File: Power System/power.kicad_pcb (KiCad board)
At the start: 2 copper layers, 139.7 x 100.3 mm, 35 parts, among them J1 PC104_40Pin_2.54mm, J2 Charge Cable, J3 Battery Pack, J4 IDC Header, U1 ds2781e+

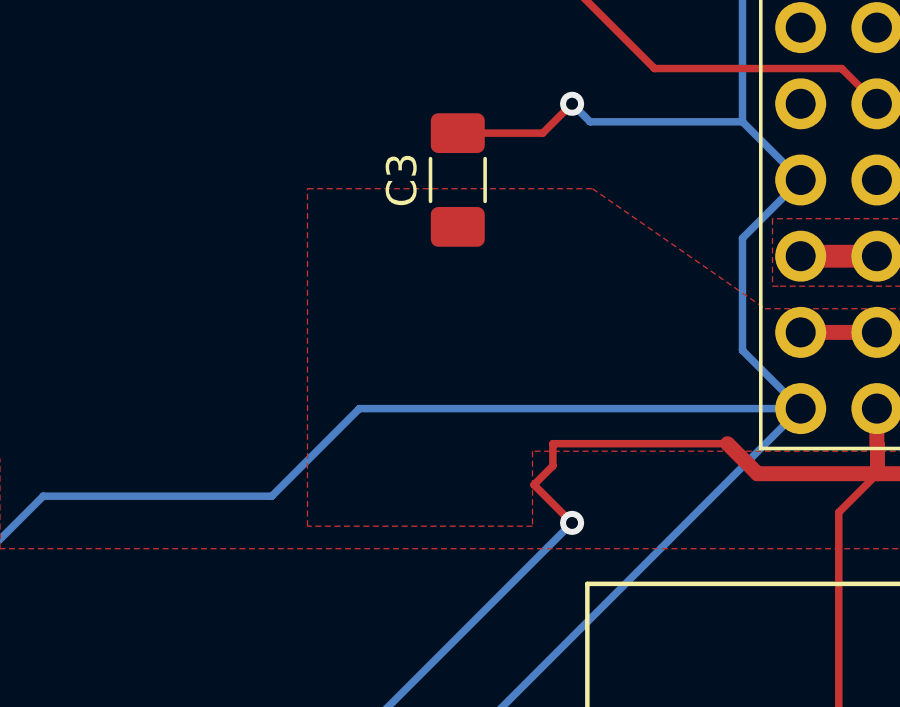
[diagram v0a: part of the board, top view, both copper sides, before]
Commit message: Further resized fill zones...
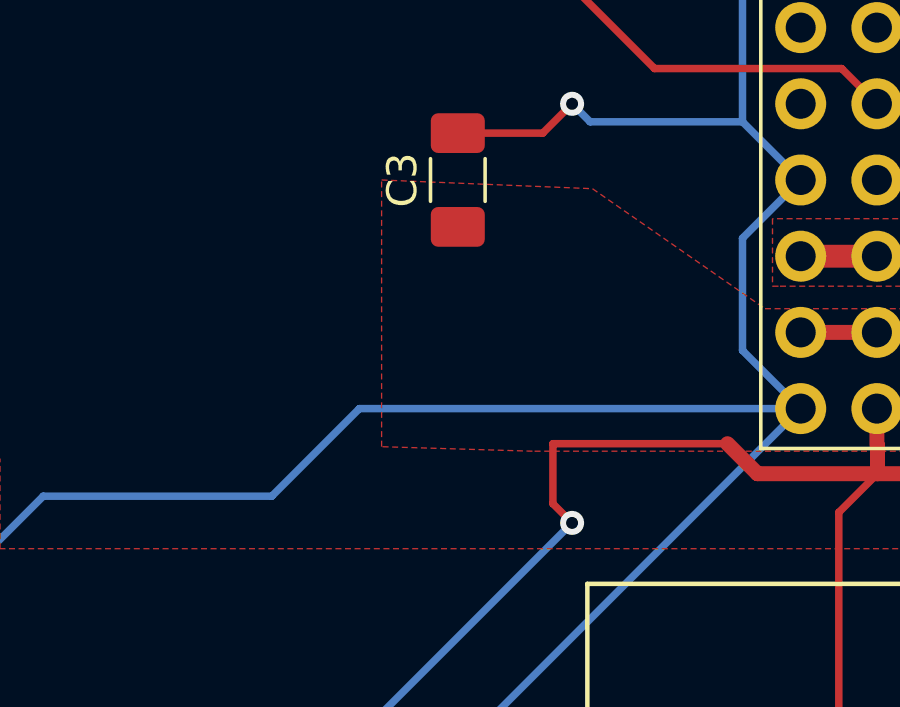
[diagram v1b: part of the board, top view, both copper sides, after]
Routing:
- net +3V3: track 156.1 -> 155.5 mm
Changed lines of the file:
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@@
     (thickness 1.6)
     (drawings 14)
-    (tracks 248)
+    (tracks 247)
     (zones 0)
     (modules 35)
@@
   (segment (start 159.5 101.75) (end 158.75 102.5) (width 0.5) (layer F.Cu) (net 23))
   (segment (start 153.5 102.5) (end 152.5 101.5) (width 0.5) (layer F.Cu) (net 23))
-  (segment (start 152.5 101.5) (end 146.68 101.5) (width 0.25) (layer F.Cu) (net 23))
   (segment (start 157.5 101.552081) (end 157.5 102.5) (width 0.5) (layer F.Cu) (net 23))
   (segment (start 157.48 101.532081) (end 157.5 101.552081) (width 0.25) (layer F.Cu) (net 23))
@@
   (via (at 147.32 104.14) (size 0.8) (drill 0.4) (layers F.Cu B.Cu) (net 23))
   (segment (start 138.5 112.96) (end 147.32 104.14) (width 0.25) (layer B.Cu) (net 23))
-  (segment (start 147.32 104.14) (end 146.05 102.87) (width 0.25) (layer F.Cu) (net 23))
-  (segment (start 146.68 101.5) (end 146.68 102.24) (width 0.25) (layer F.Cu) (net 23))
-  (segment (start 146.68 102.24) (end 146.05 102.87) (width 0.25) (layer F.Cu) (net 23))
+  (segment (start 146.68 103.5) (end 147.32 104.14) (width 0.25) (layer F.Cu) (net 23))
+  (segment (start 146.68 101.5) (end 146.68 103.5) (width 0.25) (layer F.Cu) (net 23))
+  (segment (start 152.5 101.5) (end 146.68 101.5) (width 0.25) (layer F.Cu) (net 23))
   (segment (start 42 67.5) (end 37.75 63.25) (width 0.25) (layer F.Cu) (net 24) (status 20))
   (segment (start 42 73.25) (end 42 67.5) (width 0.25) (layer F.Cu) (net 24))
@@
     (polygon
       (pts
-        (xy 138.5 104.25) (xy 138.5 93) (xy 148 93) (xy 153.75 97) (xy 158.75 97)
-        (xy 158.75 101.75) (xy 146 101.75) (xy 146 104.25)
+        (xy 140.97 101.6) (xy 140.97 92.71) (xy 148 93) (xy 153.75 97) (xy 158.75 97)
+        (xy 158.75 101.75) (xy 146 101.75)
       )
     )

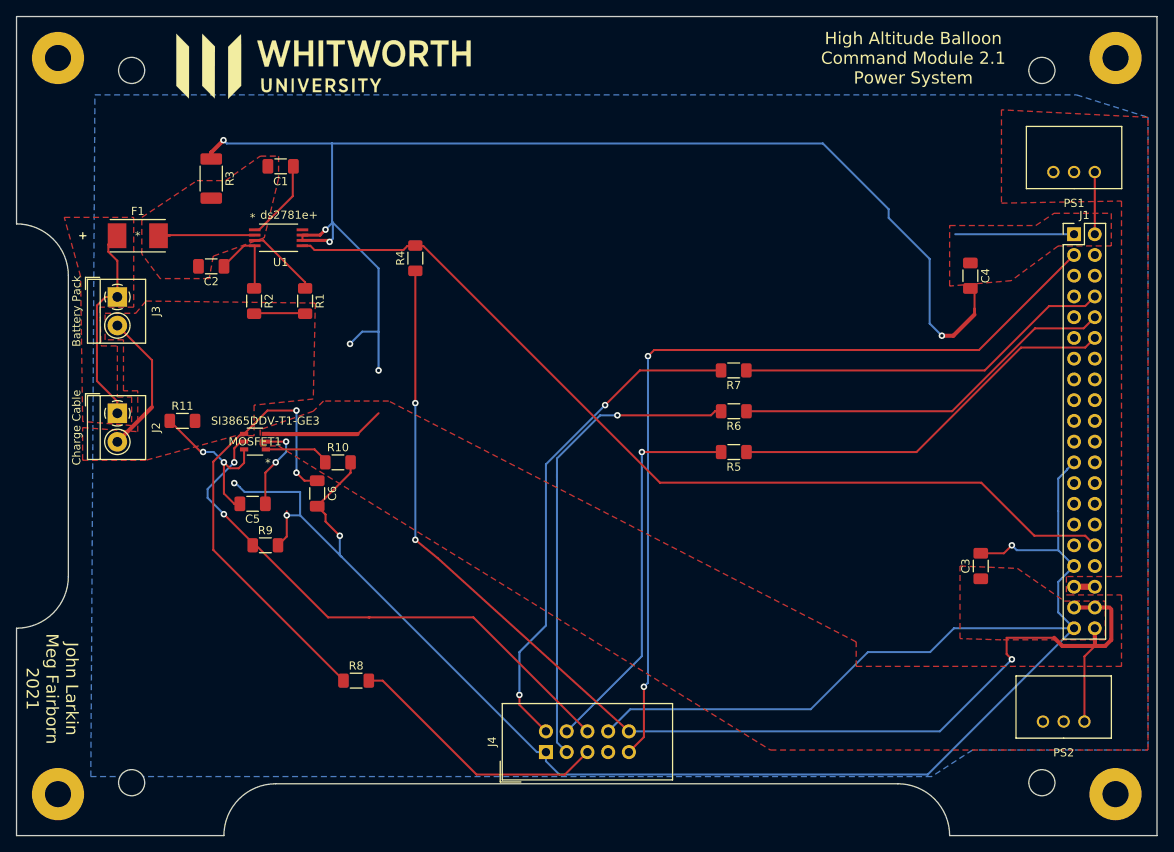
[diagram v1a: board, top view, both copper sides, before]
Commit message: Pretty sure power system fill zones are done
I don't know why it wants to commit changes to the schematic?
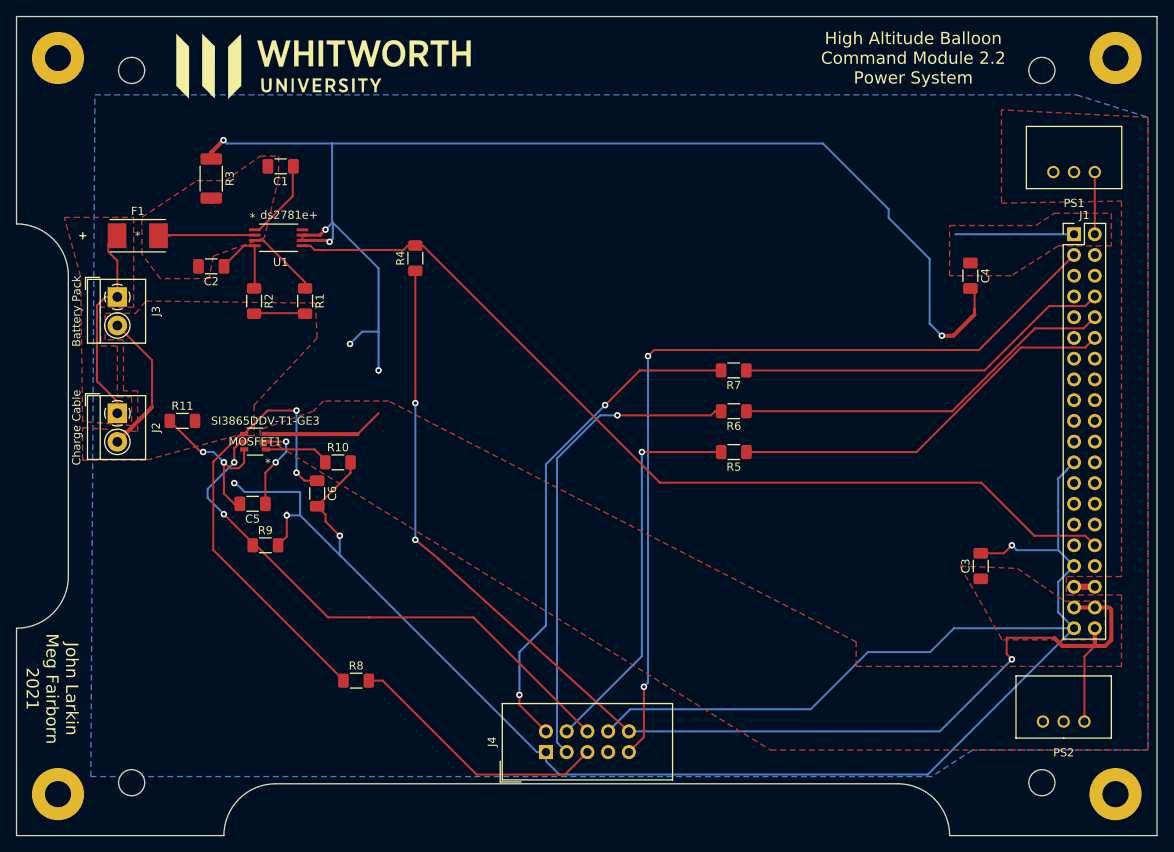
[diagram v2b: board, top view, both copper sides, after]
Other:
- board text added: "High Altitude Balloon Command Module 2.2 Power System"
- board text removed: "High Altitude Balloon Command Module 2.1 Power System"

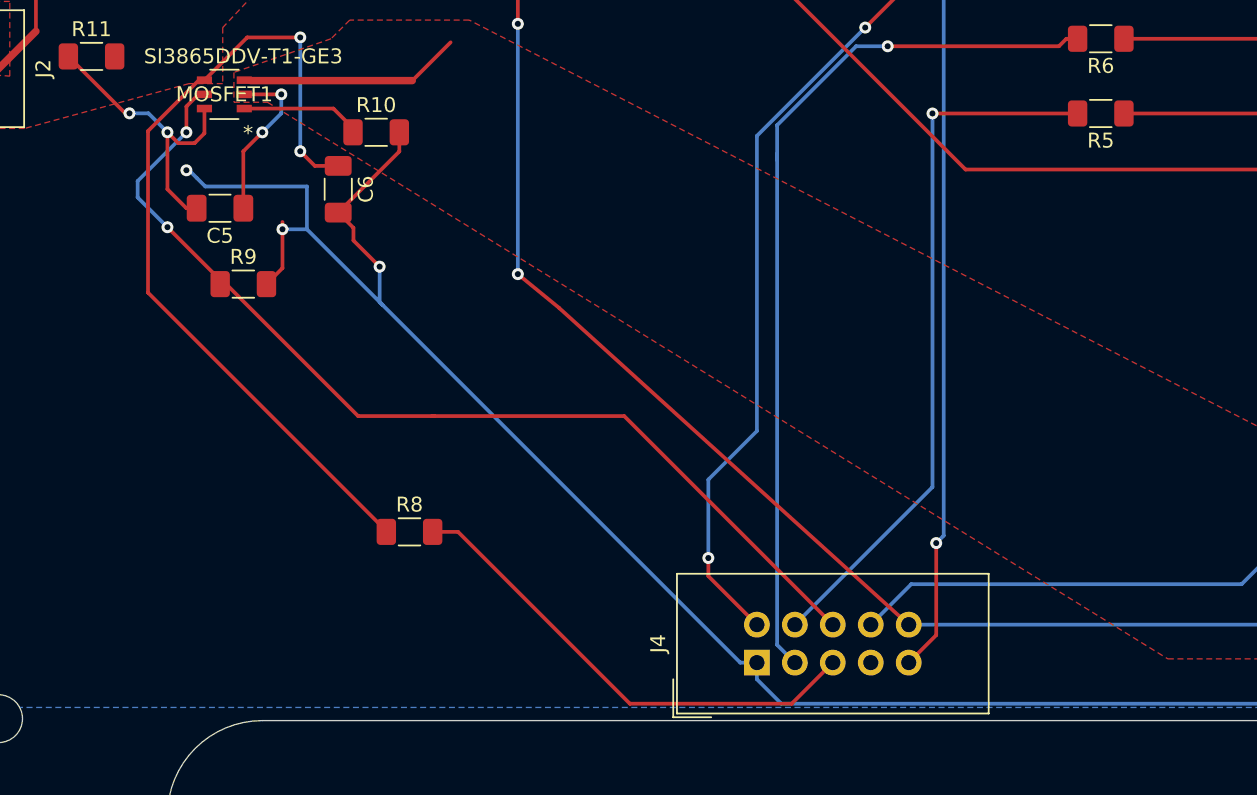
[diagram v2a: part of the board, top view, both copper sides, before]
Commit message: moved components away from each other
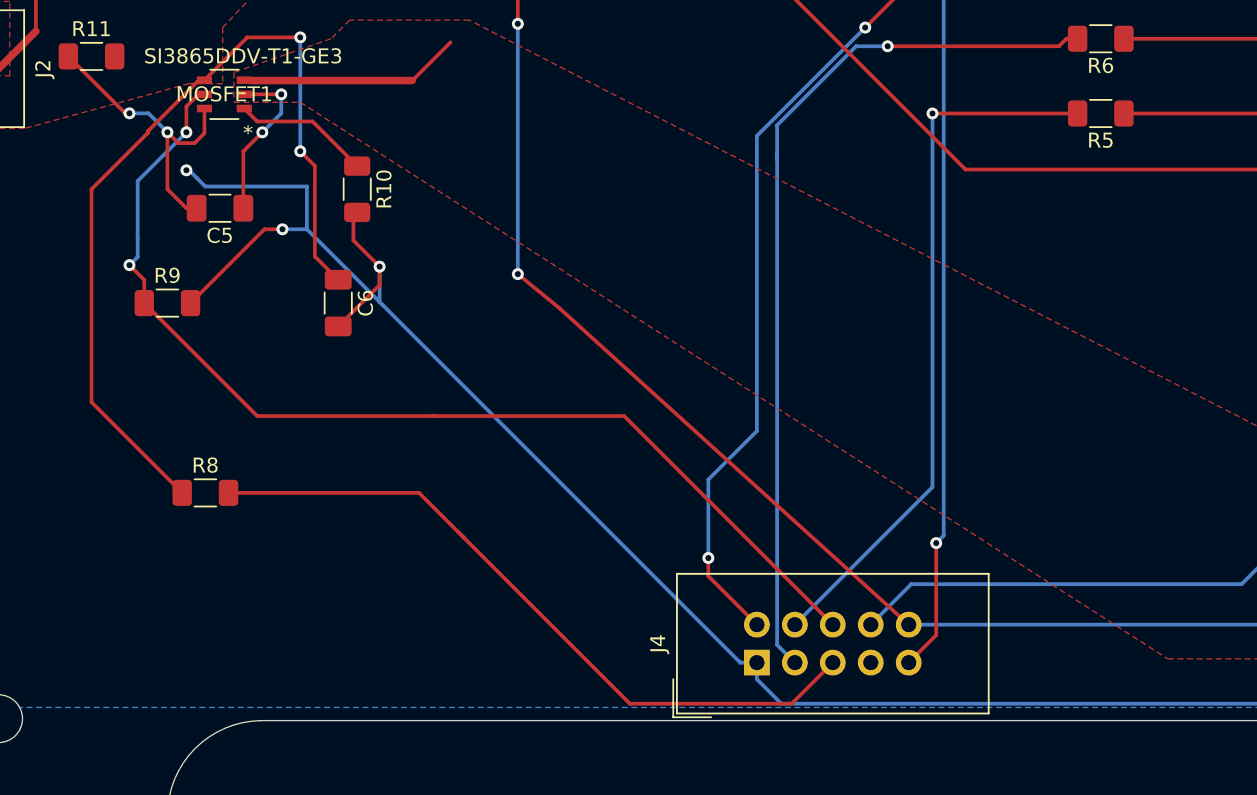
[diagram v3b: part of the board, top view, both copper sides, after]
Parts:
- moved R8 13.9 mm to (53.3, 104.1)
- moved C6 7.62 mm to (62.2, 91.4)
- moved R9 5.24 mm to (50.8, 91.4)
- moved R10 4.02 mm to (63.5, 83.8), turned to 270 degrees
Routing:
- net Net-(J4-Pad5): track 32.7 -> 48.0 mm
- net /PWR_ENABLE: track 67.7 -> 71.9 mm
- net +BATT: track 80.4 -> 82.0 mm
- net GND: track 419.2 -> 420.3 mm
- net Net-(MOSFET1-Pad1): track 8.10 -> 9.15 mm

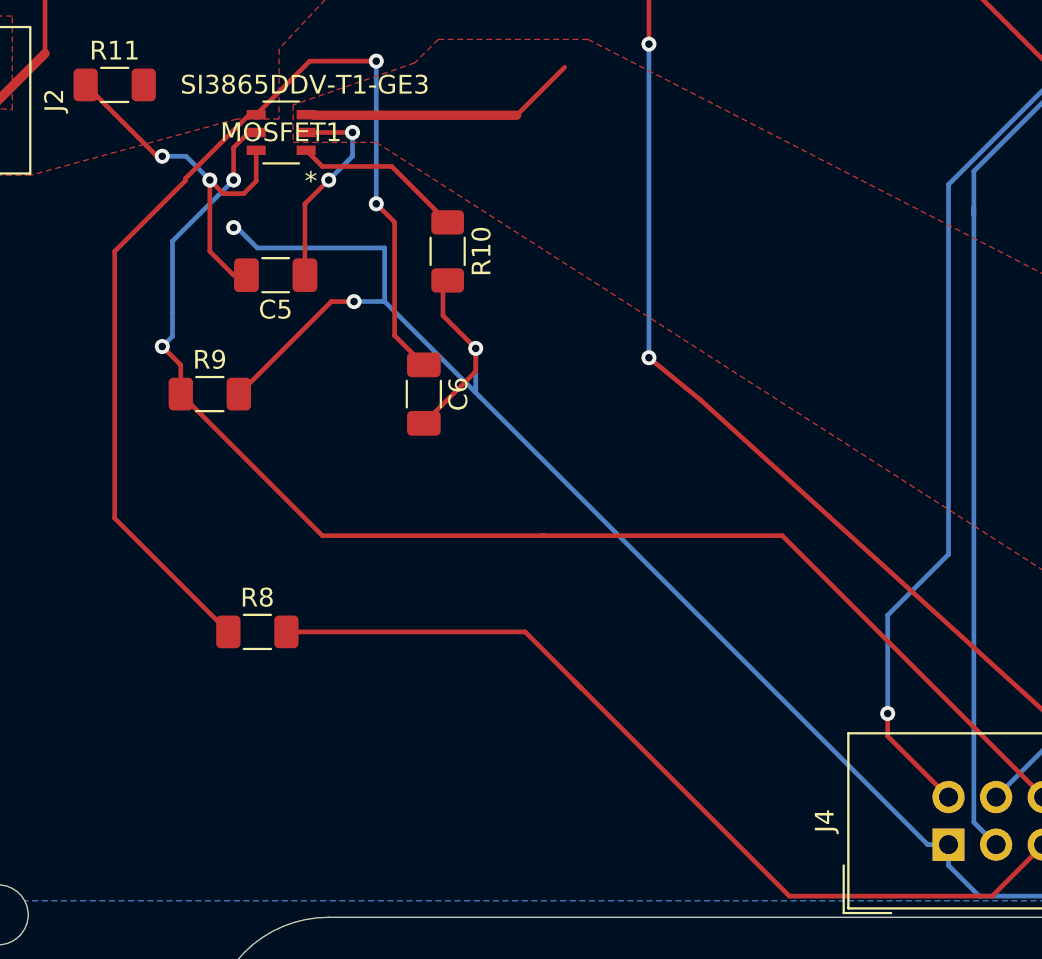
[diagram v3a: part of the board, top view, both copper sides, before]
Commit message: moved C6 a little more and changed track layout a little
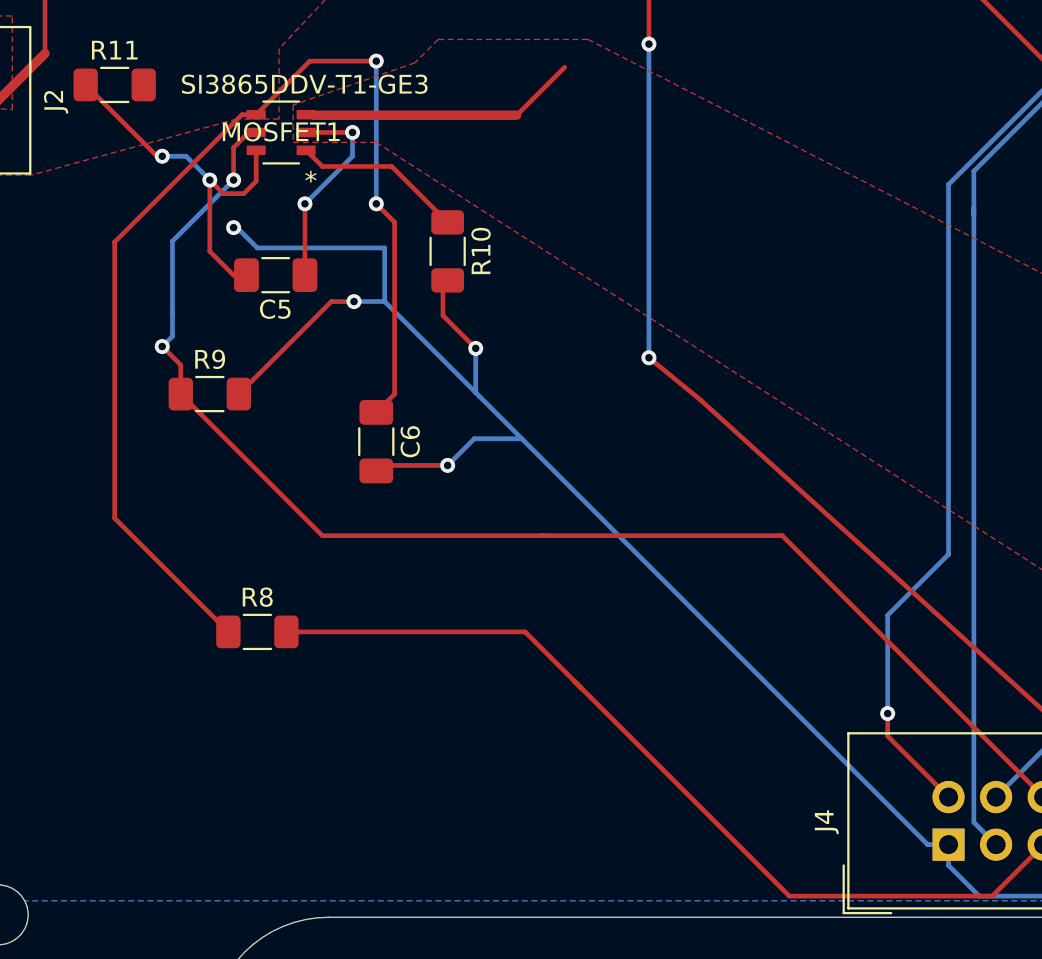
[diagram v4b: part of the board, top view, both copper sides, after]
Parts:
- moved C6 3.59 mm to (59.7, 94.0)
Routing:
- net GND: track 420.3 -> 423.7 mm, vias 10 -> 11
- net +BATT: track 82.0 -> 84.9 mm

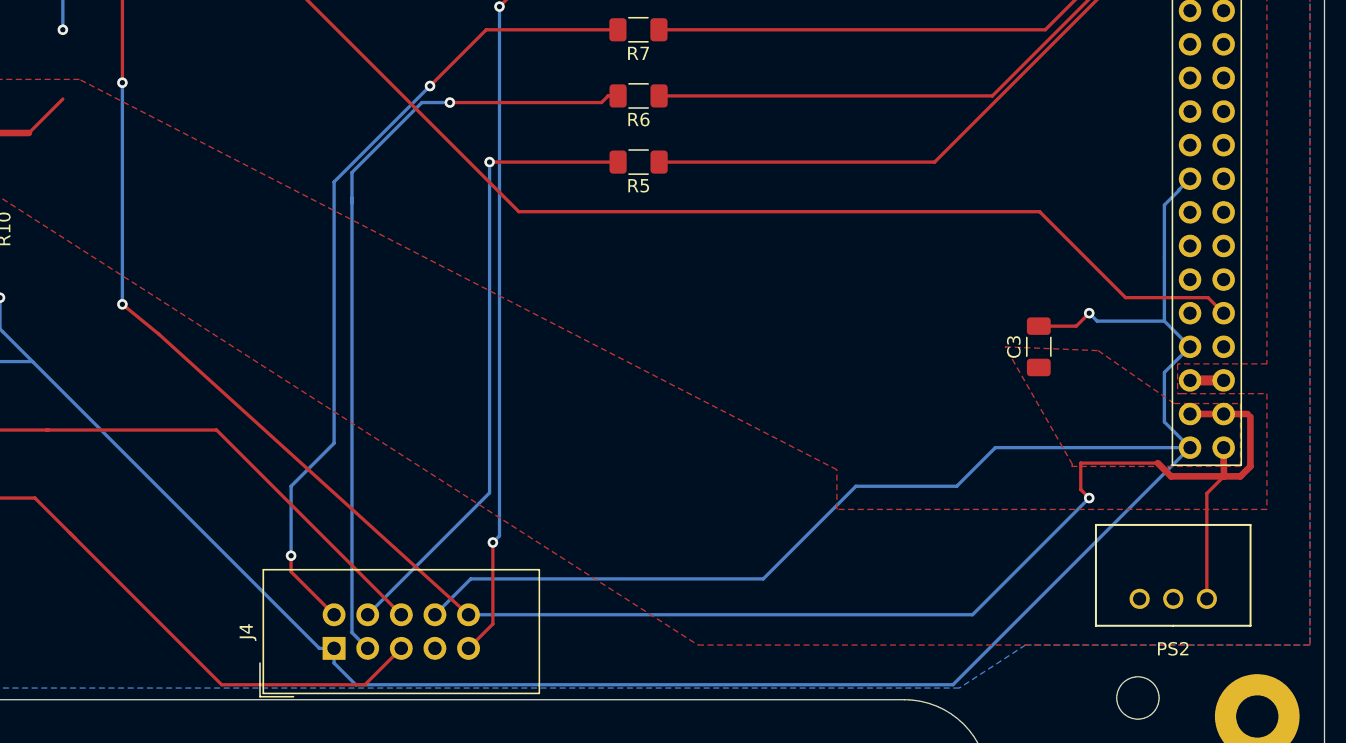
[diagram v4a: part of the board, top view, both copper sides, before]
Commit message: Improve 3.3 V fill zone
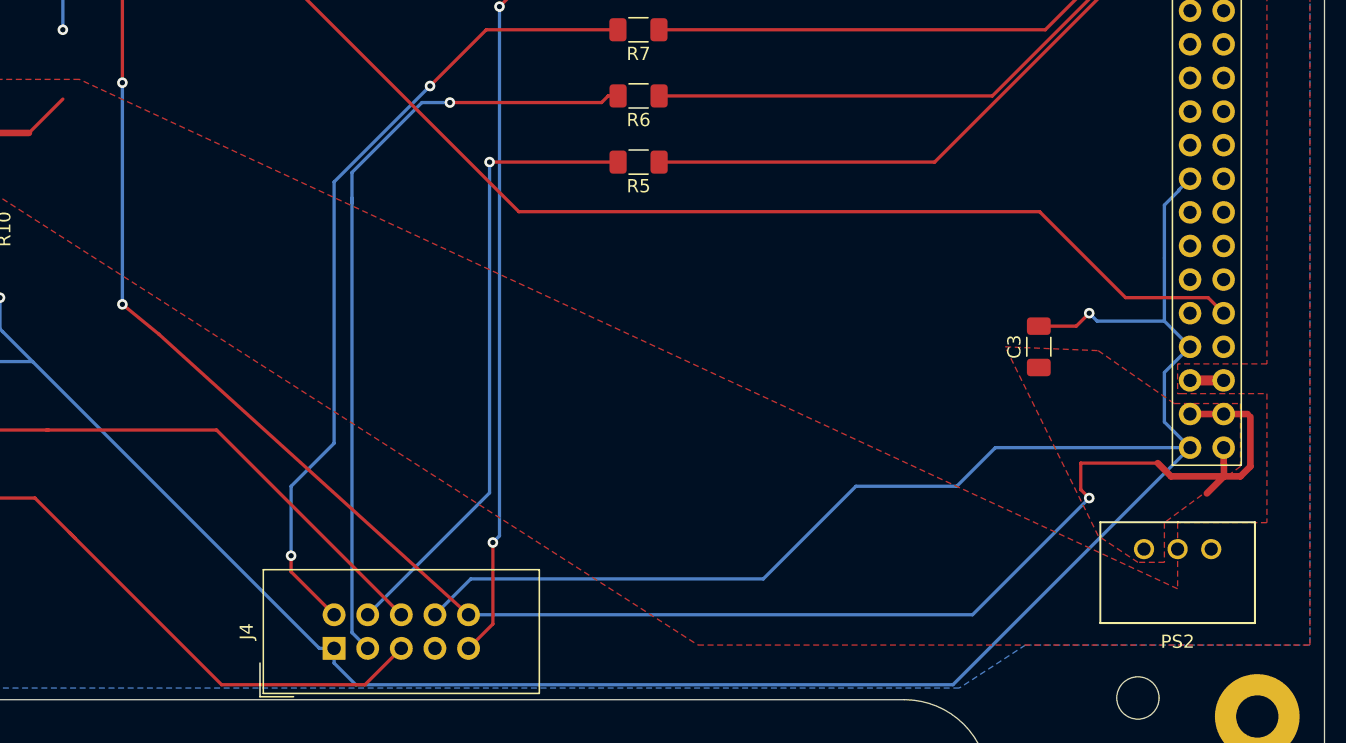
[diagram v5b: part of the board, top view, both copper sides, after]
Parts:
- moved PS2 3.77 mm to (154.0, 108.0), turned to 180 degrees
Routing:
- net +3V3: track 155.5 -> 147.6 mm

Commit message: Fill zone rework
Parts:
- MOSFET1: value SI3865DDV-T1-GE3 -> SI3865DDV
- moved C6 25.0 mm to (59.0, 69.0), turned to 0 degrees
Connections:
- net /INTERBOARD_0 renamed /AUDIO_ALERT
- net /RADIO_RX renamed /USB_D+
- net /RADIO_TX renamed /USB_B-
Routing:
- net GND: track 423.7 -> 394.3 mm, vias 11 -> 8
- net +BATT: track 84.9 -> 57.7 mm, vias 2 -> 0
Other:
- board text added: "+"
